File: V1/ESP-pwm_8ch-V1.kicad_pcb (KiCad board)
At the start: 2 copper layers, 113 x 67.8 mm, 47 parts, among them J1 12VDC, J2 CH1/2, J3 CH3/4, J4 CH5/6, J5 CH7/8, Q1 IRLB8721PBF, Q2 IRLB8721PBF, Q3 IRLB8721PBF, Q4 IRLB8721PBF, Q5 IRLB8721PBF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

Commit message: Update ESP-pwm_8ch-V1.kicad_pcb
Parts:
- moved R1 12.1 mm to (67.9, 89.8)
- moved R2 3.81 mm to (78.7, 89.8)
- moved R3 3.81 mm to (81.3, 89.8)
- turned D3 to 180 degrees
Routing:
- net +12VA: track 36.5 -> 24.4 mm, vias 2 -> 0
- net +3V3: track 9.76 -> 13.5 mm
- net Net-(D3-Pad2): track 16.7 -> 14.9 mm
- net Net-(D4-Pad2): track 21.5 -> 20.7 mm
- net Net-(D2-Pad2): track 26.4 -> 27.0 mm

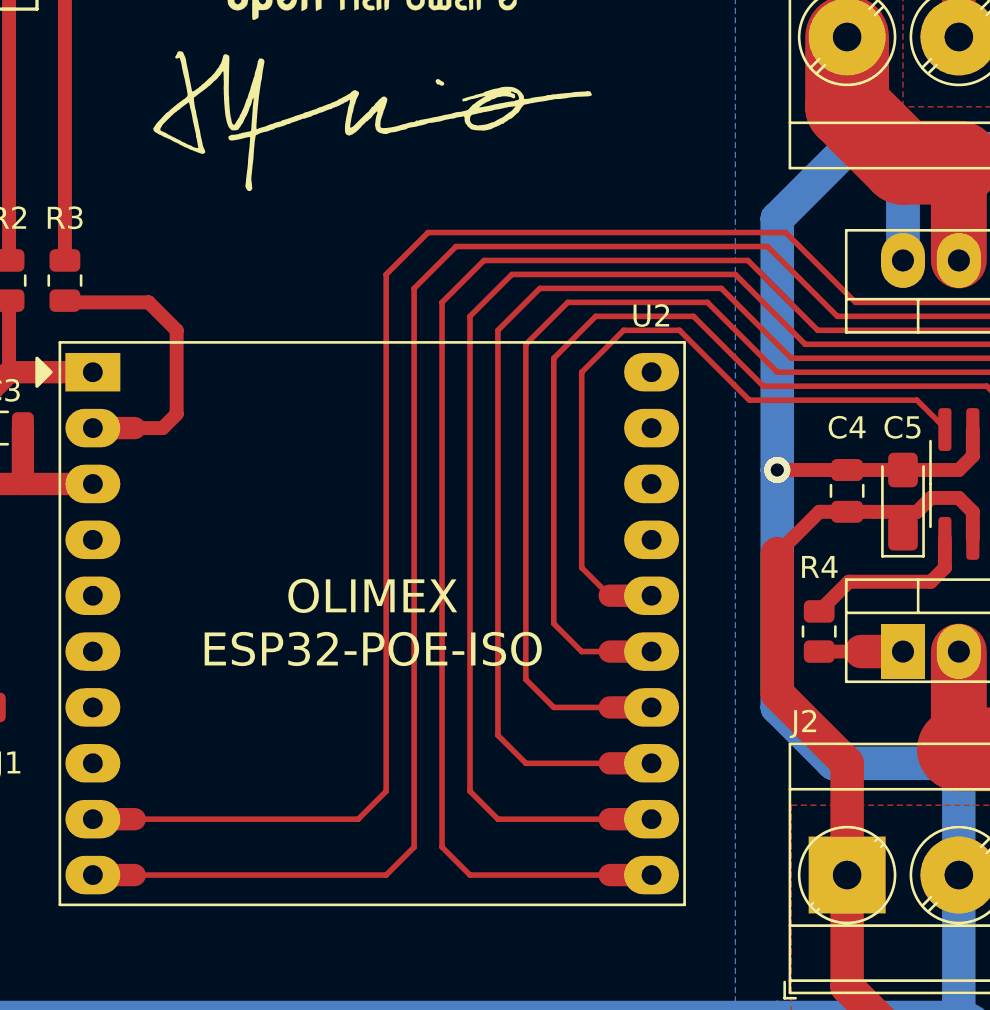
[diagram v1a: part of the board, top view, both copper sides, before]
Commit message: Updated MOSFET gate resistor
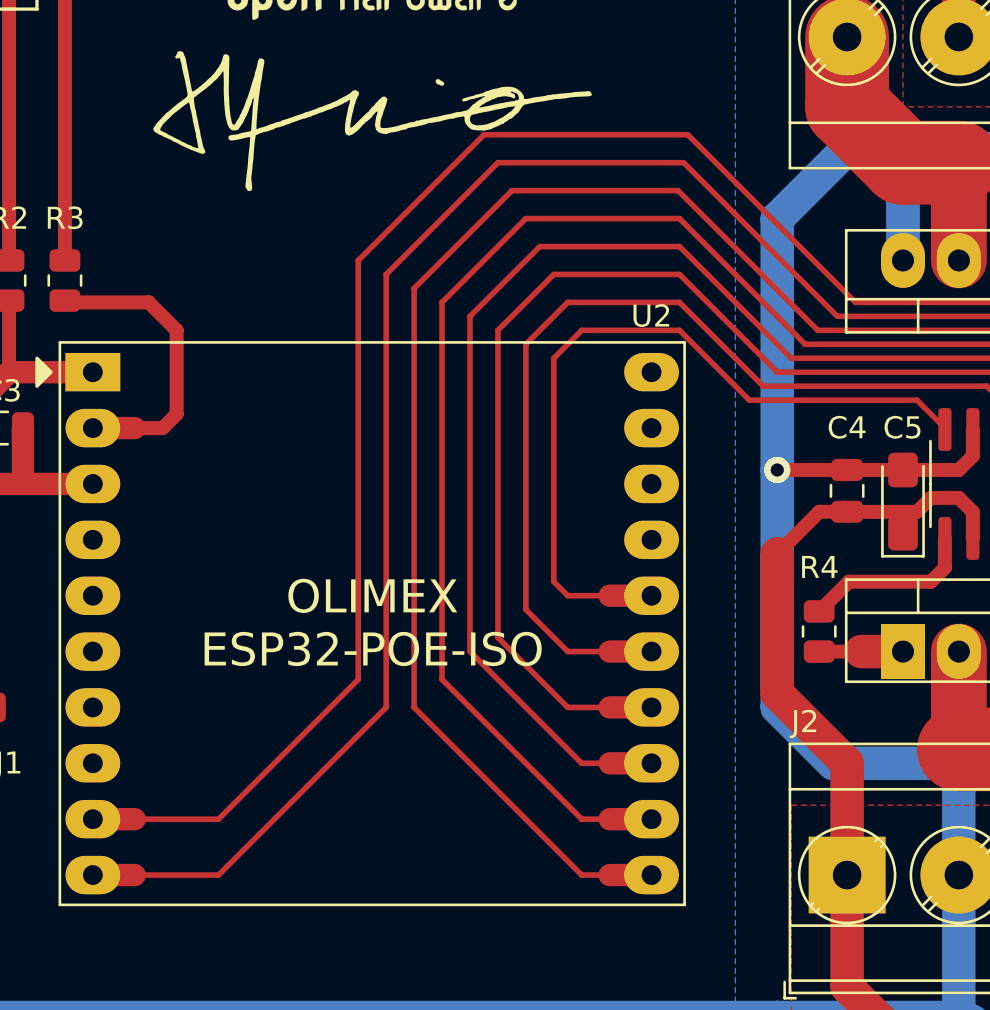
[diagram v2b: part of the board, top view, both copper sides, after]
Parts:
- R10, R11, R4, R5, R6, R7, R8, R9: value 0R/0,125W/0805 -> 22R/0,125W/0805
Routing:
- net Net-(U2-Pad16): track 31.7 -> 35.0 mm
- net Net-(U2-Pad15): track 41.1 -> 44.1 mm
- net Net-(U2-Pad14): track 86.5 -> 89.4 mm
- net Net-(U2-Pad13): track 95.5 -> 97.7 mm
- net Net-(U2-Pad12): track 111.3 -> 113.3 mm
- net Net-(U2-Pad11): track 119.6 -> 121.4 mm
- net Net-(U2-Pad9): track 82.4 -> 83.5 mm

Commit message: Added ESP8266
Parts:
- added R12: 4k7/0,125W/0805, Tales:R_0805_2012Metric, F.Cu at (79.4, 101.9)
- added U2: WeMos_D1_mini, Tales:WEMOS_D1_mini_light_pads, F.Cu at (83.8, 67.3)
- moved G*** 39.4 mm to (95.2, 121.9)
- moved REF** 39.4 mm to (95.2, 111.8)
- renumbered U2 to U3, U3 to U4, U4 to U5, U5 to U6, U6 to U7
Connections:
- U3 pad 4: unconnected-(U2-Pad4) -> Net-(U3-Pad4)
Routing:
- net +5V: track 12.6 -> 55.2 mm, vias 0 -> 4
- net GNDREF: track 465.9 -> 506.5 mm, vias 4 -> 6
- net Net-(U2-Pad5): track 35.0 -> 72.5 mm, vias 0 -> 2
- net Net-(U2-Pad4): track 44.1 -> 80.3 mm, vias 0 -> 2
- net Net-(U2-Pad14): track 97.7 -> 122.2 mm, vias 0 -> 2
- net Net-(U2-Pad13): track 89.4 -> 111.8 mm, vias 0 -> 2
- net +3V3: track 13.5 -> 25.5 mm, vias 0 -> 1
- net Net-(U7-Pad2): track 83.5 -> 79.8 mm
- net Net-(U3-Pad4): track 0.00 -> 3.67 mm
- net Net-(U7-Pad4): track 90.3 -> 87.2 mm
- net Net-(U3-Pad11): track 121.4 -> 118.8 mm
- net Net-(U6-Pad2): track 113.3 -> 111.2 mm
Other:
- board text added: "WEMOS D1 MINI"

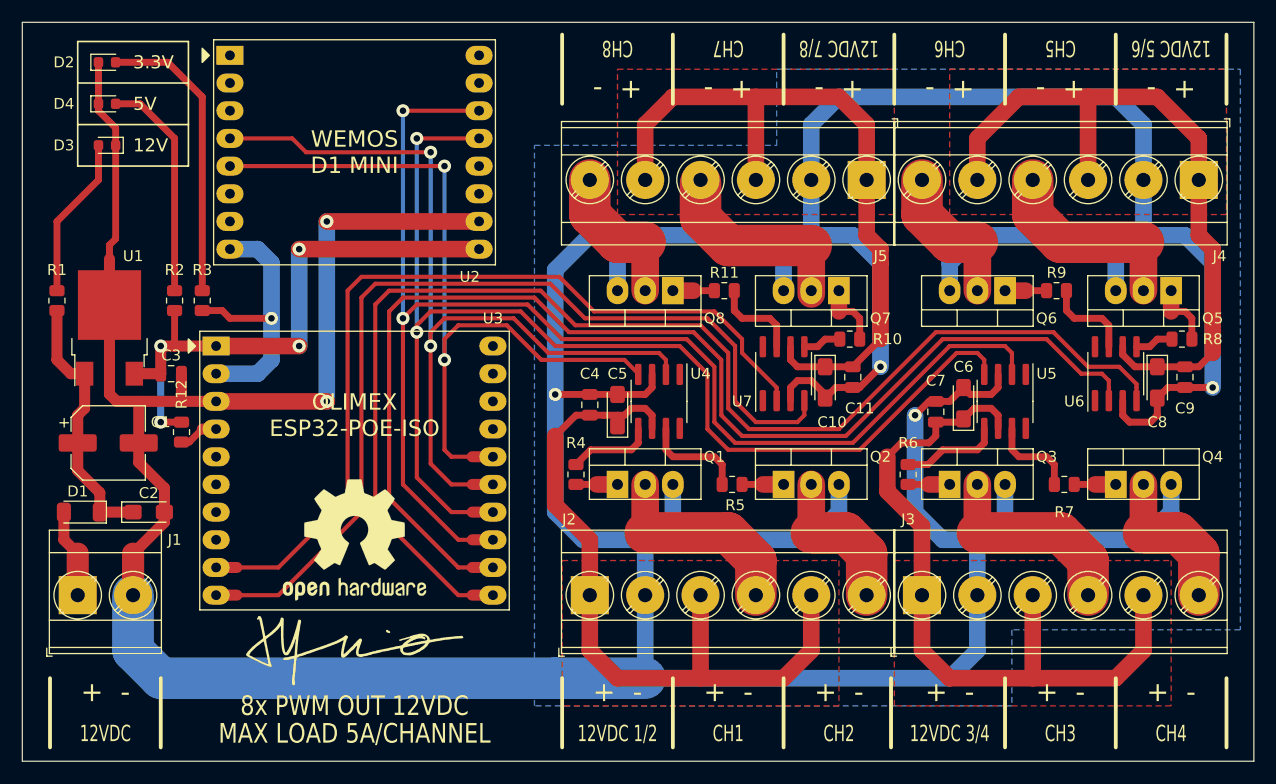
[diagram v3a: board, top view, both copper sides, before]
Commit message: Reset pull up to +3.3V
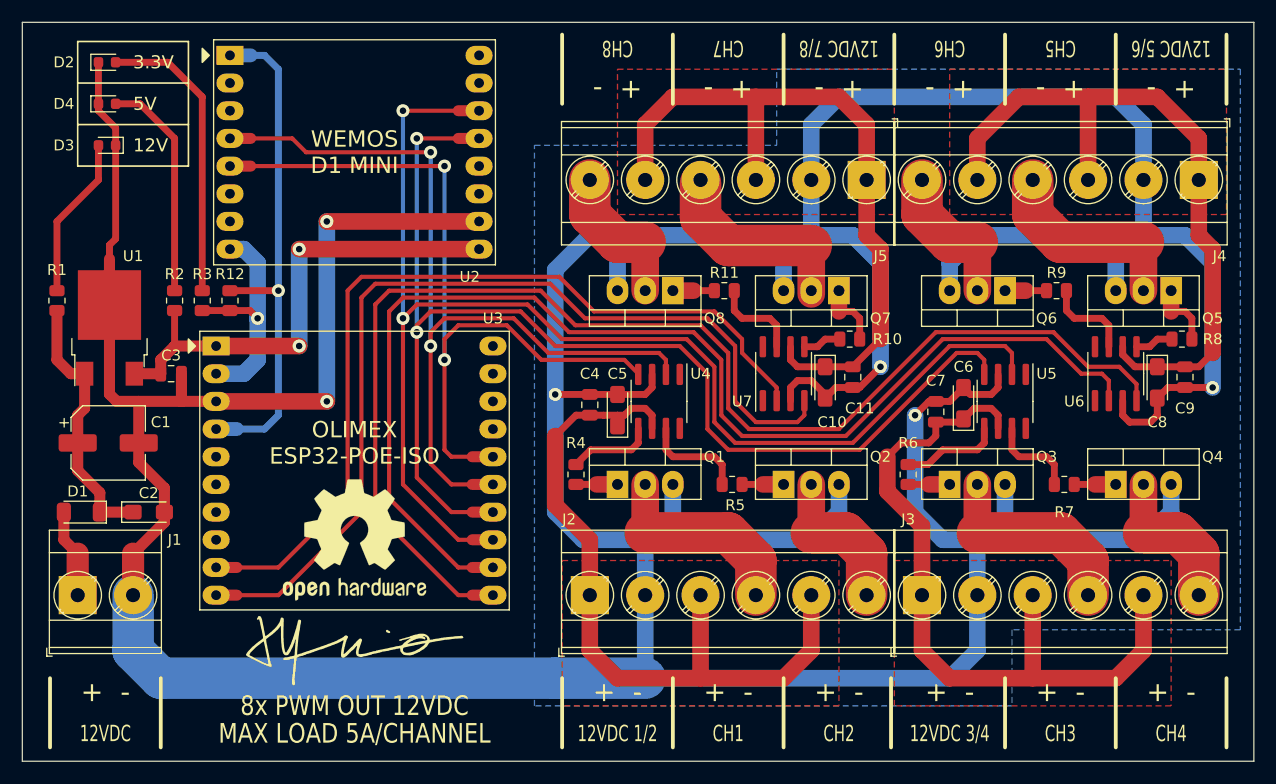
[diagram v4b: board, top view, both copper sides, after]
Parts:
- moved R12 12.9 mm to (83.8, 89.8), turned to 90 degrees
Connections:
- R12 pad 1: +5V -> +3V3
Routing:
- net Net-(R12-Pad2): track 3.67 -> 47.4 mm, vias 0 -> 1
- net +5V: track 55.2 -> 45.6 mm, vias 4 -> 2
- net +3V3: track 25.5 -> 21.7 mm
